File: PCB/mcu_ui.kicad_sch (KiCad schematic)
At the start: 32 parts, among them J5 UPDI, SW1 EC11E18244A5, SW2 BAND, SW3 STEP, SW4 MENU, U4 ATtiny3226-SU

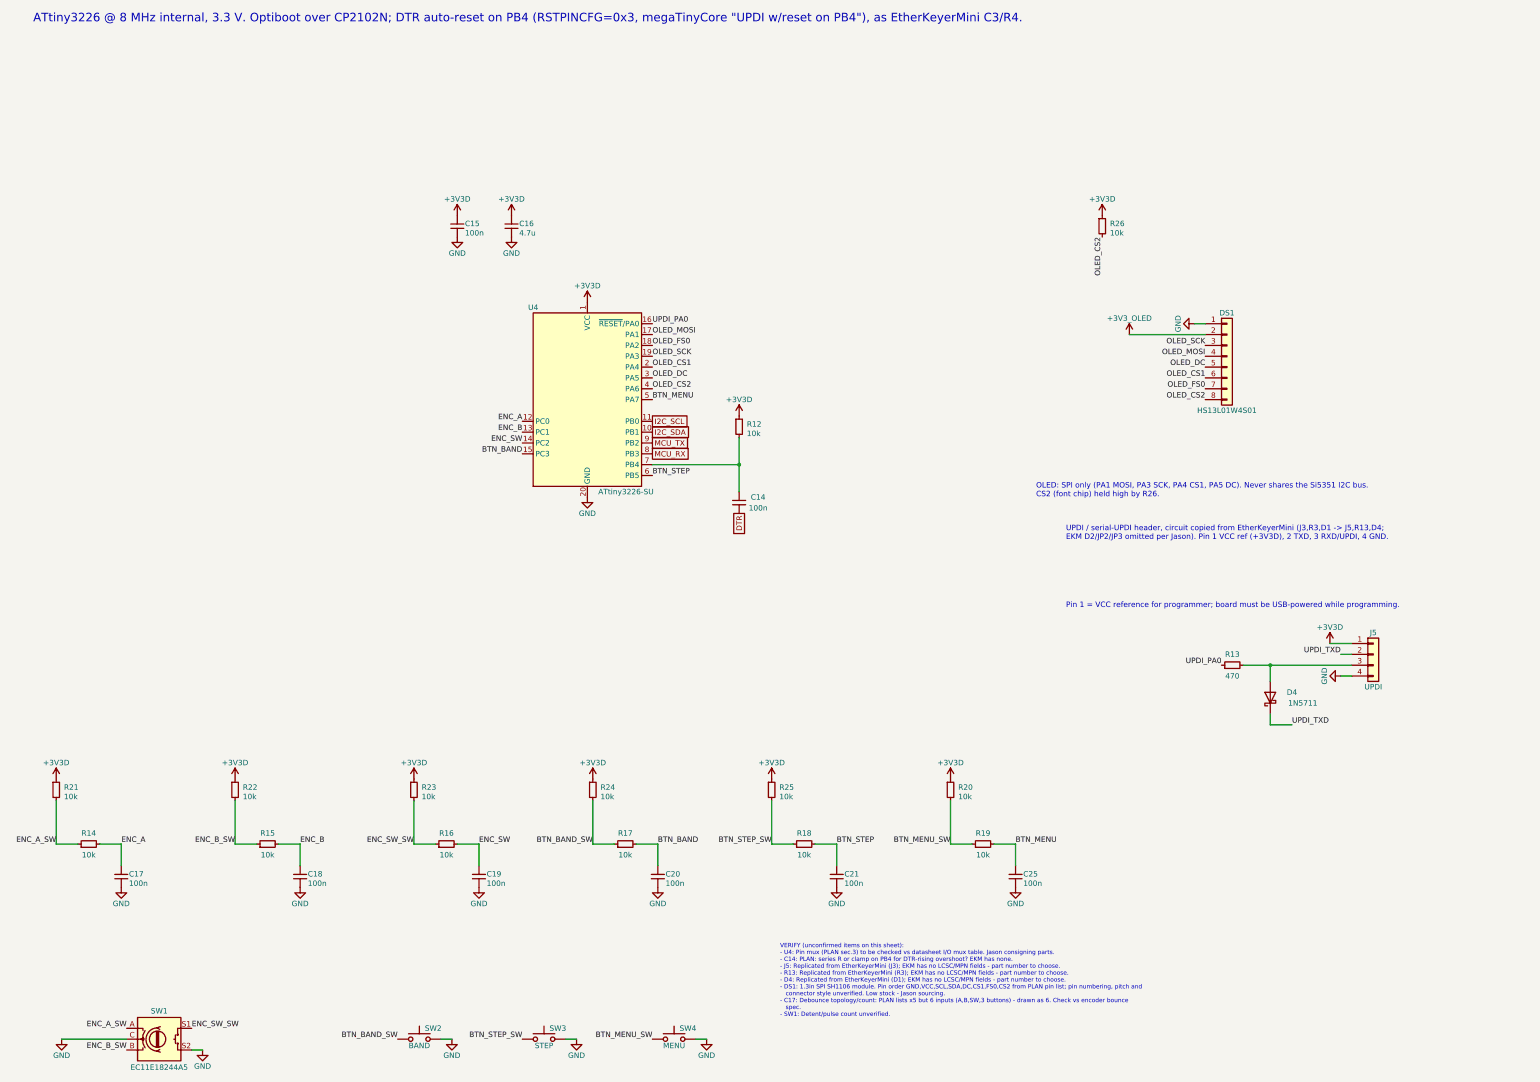
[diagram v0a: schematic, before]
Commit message: Schematic: US resistor symbols, decoupling caps at their ICs, drop finalized VERIFY notes
- Device:R_Small -> Device:R_Small_US on all 30 resistors (same pin geometry; refs/values/fields/footprints/LCSC unchanged)
- Move label-connected decoupling caps next to their ICs: C10/C11 + C12/C13 at U3, C15/C16 at U4, C4 at U2
- Add PCB placement notes by U1, U5, U3, U4, U2/X1 and DS1 (pins from netlist)
- Remove VERIFY note lines and VERIFY fields for items Jason finalized:
  J1 D1 C10 U3 FB2 DS1 C17 SW1 X1 C100 R101 L1 C105
- Netlist identical to 4963a6d; ERC 0 errors
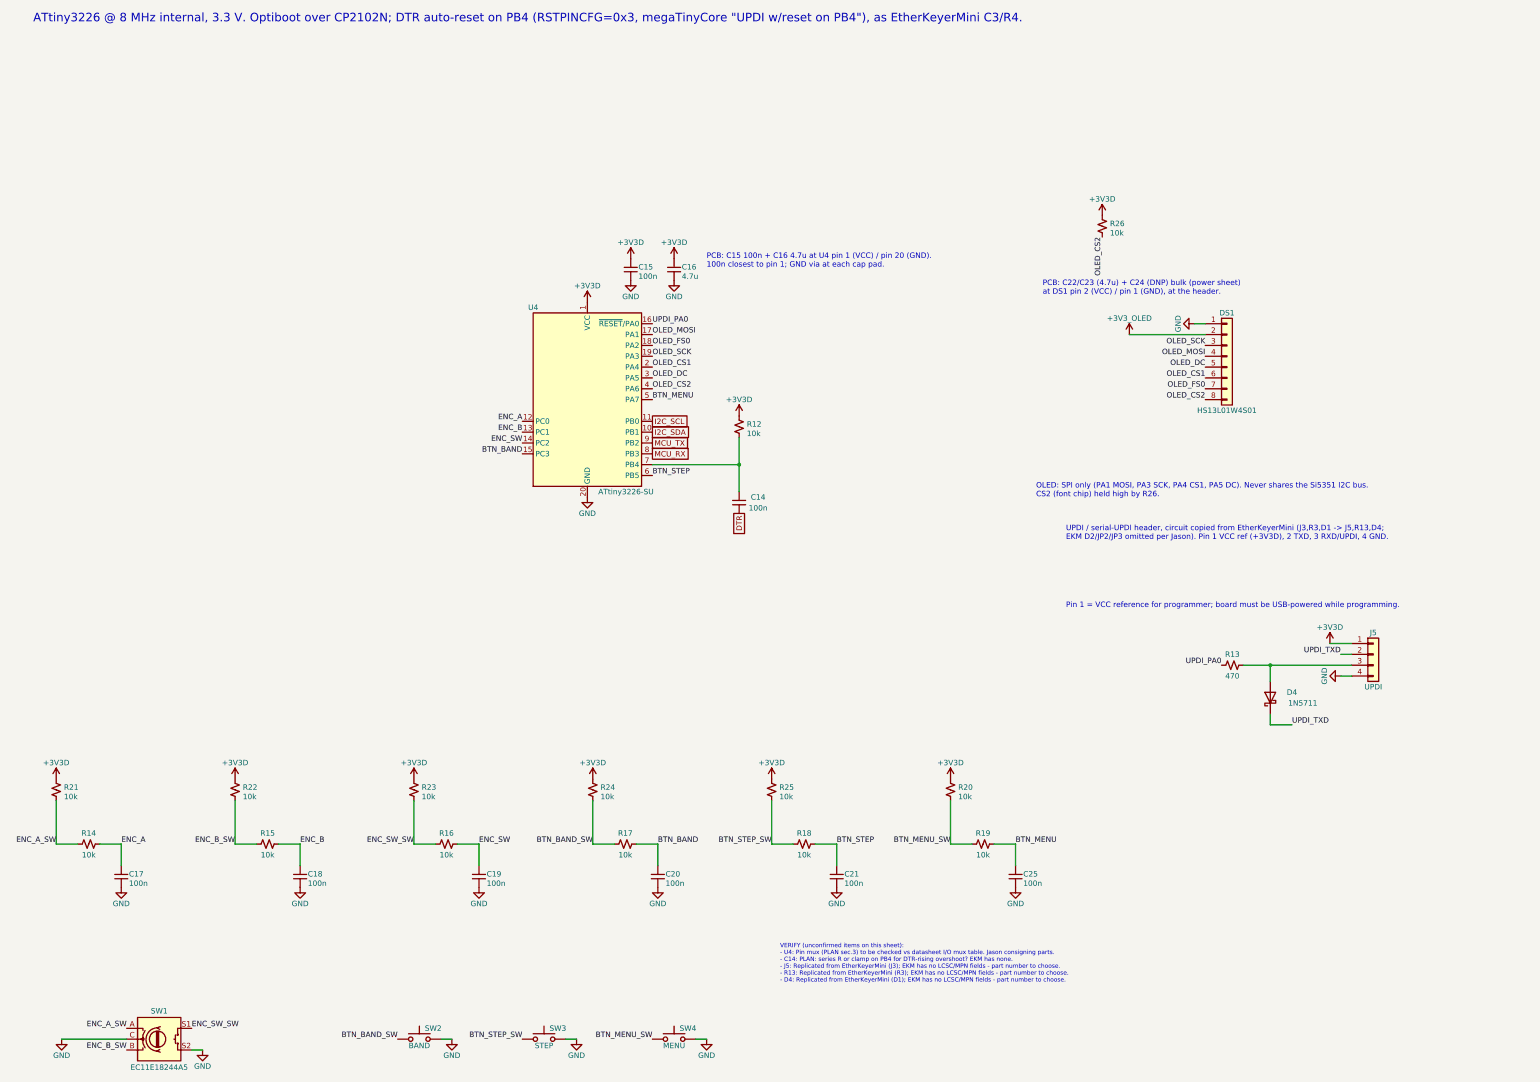
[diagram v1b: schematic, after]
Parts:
- C17: VERIFY Debounce topology/count: PLAN lists x5 but 6 inputs (A,B,SW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 -> (none)
- DS1: VERIFY 1.3in SPI SH1106 module. Pin order GND,VCC,SCL,SDA,DC,CS1,F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 -> (none)
- R12, R13, R14, R15, R16, R17, R18, R19, R20, R21, R22, R23, R24, R25, R26: symbol Device:R_Small -> Device:R_Small_US
- SW1: VERIFY Detent/pulse count unverified. -> (none)
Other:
- note added: "PCB: C15 100n + C16 4.7u at U4 pin 1 (VCC) / pin 20 (GND). 100n closest to pin 1; GND via at each cap pad."
- note added: "PCB: C22/C23 (4.7u) + C24 (DNP) bulk (power sheet) at DS1 pin 2 (VCC) / pin 1 (GND), at the header."
- moved on the sheet: C15, C16
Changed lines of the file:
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@@
 		)
 	)
-	(text "VERIFY (unconfirmed items on this sheet):\n- U4: Pin mux (PLAN sec.3) to be checked vs datasheet I/O mux table. Jason consigning parts.\n- C14: PLAN: series R or clamp on PB4 for DTR-rising overshoot? EKM has none.\n- J5: Replicated from EtherKeyerMini (J3); EKM has no LCSC/MPN fields - part number to choose.\n- R13: Replicated from EtherKeyerMini (R3); EKM has no LCSC/MPN fields - part number to choose.\n- D4: Replicated from EtherKeyerMini (D1); EKM has no LCSC/MPN fields - part number to choose.\n- DS1: 1.3in SPI SH1106 module. Pin order GND,VCC,SCL,SDA,DC,CS1,FS0,CS2 from PLAN pin list; pin numbering, pitch and\n   connector style unverified. Low stock - Jason sourcing.\n- C17: Debounce topology/count: PLAN lists x5 but 6 inputs (A,B,SW,3 buttons) - drawn as 6. Check vs encoder bounce\n   spec.\n- SW1: Detent/pulse count unverified."
+	(text "VERIFY (unconfirmed items on this sheet):\n- U4: Pin mux (PLAN sec.3) to be checked vs datasheet I/O mux table. Jason consigning parts.\n- C14: PLAN: series R or clamp on PB4 for DTR-rising overshoot? EKM has none.\n- J5: Replicated from EtherKeyerMini (J3); EKM has no LCSC/MPN fields - part number to choose.\n- R13: Replicated from EtherKeyerMini (R3); EKM has no LCSC/MPN fields - part number to choose.\n- D4: Replicated from EtherKeyerMini (D1); EKM has no LCSC/MPN fields - part number to choose."
 		(exclude_from_sim no)
 		(at 195 238 0)
@@
 		)
 	)
+	(text "PCB: C15 100n + C16 4.7u at U4 pin 1 (VCC) / pin 20 (GND).\n100n closest to pin 1; GND via at each cap pad."
+		(exclude_from_sim no)
+		(at 177.8 76.2 0)
+		(effects
+			(font
+				(size 1.27 1.27)
+			)
+			(justify left top)
+		)
+	)
+	(text "PCB: C22/C23 (4.7u) + C24 (DNP) bulk (power sheet)\nat DS1 pin 2 (VCC) / pin 1 (GND), at the header."
+		(exclude_from_sim no)
+		(at 256.54 82.55 0)
+		(effects
+			(font
+				(size 1.27 1.27)
+			)
+			(justify left top)
+		)
+	)
 	(junction
 		(at 185.42 125.73)
@@
 	(symbol
 		(lib_id "Device:C_Small")
-		(at 132.08 69.85 0)
+		(at 170.18 80.01 0)
 		(unit 1)
 		(body_style 1)
@@
 		(dnp no)
 		(property "Reference" "C16"
-			(at 133.88 69.25 0)
+			(at 171.98 79.41 0)
 			(show_name no)
 			(do_not_autoplace no)
@@
 		)
 		(property "Value" "4.7u"
-			(at 133.88 71.45 0)
+			(at 171.98 81.61 0)
 			(show_name no)
 			(do_not_autoplace no)
@@
 		)
 		(property "Footprint" "Capacitor_SMD:C_0805_2012Metric"
-			(at 132.08 69.85 0)
+			(at 170.18 80.01 0)
 			(hide yes)
 			(show_name no)
@@
 		)
 		(property "Datasheet" ""
-			(at 132.08 69.85 0)
+			(at 170.18 80.01 0)
 			(hide yes)
 			(show_name no)
@@
 		)
 		(property "Description" "Unpolarized capacitor, small symbol"
-			(at 132.08 69.85 0)
+			(at 170.18 80.01 0)
 			(hide yes)
 			(show_name no)
@@
 		)
 		(property "LCSC" "C1779"
-			(at 132.08 69.85 0)
+			(at 170.18 80.01 0)
 			(hide yes)
 			(show_name no)
@@
 		)
 		(property "MPN" "CL21A475KAQNNNE"
-			(at 132.08 69.85 0)
+			(at 170.18 80.01 0)
 			(hide yes)
 			(show_name no)
@@
 		)
 		(property "Manufacturer" "Samsung"
-			(at 132.08 69.85 0)
+			(at 170.18 80.01 0)
 			(hide yes)
 			(show_name no)
@@
 	)
 	(symbol
-		(lib_id "Device:R_Small")
+		(lib_id "Device:R_Small_US")
 		(at 300.99 172.72 90)
 		(unit 1)
@@
 	(symbol
 		(lib_id "power:+3V3")
-		(at 119.38 67.31 0)
+		(at 160.02 77.47 0)
 		(unit 1)
 		(body_style 1)
@@
 		(dnp no)
 		(property "Reference" "#PWR053"
-			(at 119.38 67.31 0)
+			(at 160.02 77.47 0)
 			(hide yes)
 			(show_name no)
@@
 		)
 		(property "Value" "+3V3D"
-			(at 119.38 63.5 0)
+			(at 160.02 73.66 0)
 			(show_name no)
 			(do_not_autoplace no)
@@
 		)
 		(property "Footprint" ""
-			(at 119.38 67.31 0)
+			(at 160.02 77.47 0)
 			(hide yes)
 			(show_name no)
@@
 		)
 		(property "Datasheet" ""
-			(at 119.38 67.31 0)
+			(at 160.02 77.47 0)
 			(hide yes)
 			(show_name no)
@@
 		)
 		(property "Description" ""
-			(at 119.38 67.31 0)
+			(at 160.02 77.47 0)
 			(show_name no)
 			(do_not_autoplace no)
@@
 	)
 	(symbol
-		(lib_id "Device:R_Small")
+		(lib_id "Device:R_Small_US")
 		(at 193.04 201.93 0)
 		(unit 1)
@@
 			)
 		)
-		(property "VERIFY" "1.3in SPI SH1106 module. Pin order GND,VCC,SCL,SDA,DC,CS1,FS0,CS2 from PLAN pin list; pin numbering, pitch and connector style unverified. Low stock - Jason sourcing."
-			(at 299.72 100.33 0)
-			(hide yes)
-			(show_name no)
-			(do_not_autoplace no)
-			(effects
-				(font
-					(size 1.27 1.27)
-				)
-			)
-		)
 		(pin "1"
 		)
@@
 	)
 	(symbol
-		(lib_id "Device:R_Small")
+		(lib_id "Device:R_Small_US")
 		(at 234.95 201.93 0)
 		(unit 1)
@@
 	)
 	(symbol
-		(lib_id "Device:R_Small")
+		(lib_id "Device:R_Small_US")
 		(at 33.02 214.63 90)
 		(unit 1)
@@
 	)
 	(symbol
-		(lib_id "Device:R_Small")
+		(lib_id "Device:R_Small_US")
 		(at 242.57 214.63 90)
 		(unit 1)
@@
 	(symbol
 		(lib_id "Device:C_Small")
-		(at 119.38 69.85 0)
+		(at 160.02 80.01 0)
 		(unit 1)
 		(body_style 1)
@@
 		(dnp no)
 		(property "Reference" "C15"
-			(at 121.18 69.25 0)
+			(at 161.82 79.41 0)
 			(show_name no)
 			(do_not_autoplace no)
@@
 		)
 		(property "Value" "100n"
-			(at 121.18 71.45 0)
+			(at 161.82 81.61 0)
 			(show_name no)
 			(do_not_autoplace no)
@@
 		)
 		(property "Footprint" "Capacitor_SMD:C_0805_2012Metric"
-			(at 119.38 69.85 0)
+			(at 160.02 80.01 0)
 			(hide yes)
 			(show_name no)
@@
 		)
 		(property "Datasheet" ""
-			(at 119.38 69.85 0)
+			(at 160.02 80.01 0)
 			(hide yes)
 			(show_name no)
@@
 		)
 		(property "Description" "Unpolarized capacitor, small symbol"
-			(at 119.38 69.85 0)
+			(at 160.02 80.01 0)
 			(hide yes)
 			(show_name no)
@@
 		)
 		(property "LCSC" "C49678"
-			(at 119.38 69.85 0)
+			(at 160.02 80.01 0)
 			(hide yes)
 			(show_name no)
@@
 		)
 		(property "MPN" "CC0805KRX7R9BB104"
-			(at 119.38 69.85 0)
+			(at 160.02 80.01 0)
 			(hide yes)
 			(show_name no)
@@
 		)
 		(property "Manufacturer" "YAGEO"
-			(at 119.38 69.85 0)
+			(at 160.02 80.01 0)
 			(hide yes)
 			(show_name no)
@@
 	)
 	(symbol
-		(lib_id "Device:R_Small")
+		(lib_id "Device:R_Small_US")
 		(at 25.4 201.93 0)
 		(unit 1)
@@
 	)
 	(symbol
-		(lib_id "Device:R_Small")
+		(lib_id "Device:R_Small_US")
 		(at 185.42 116.84 0)
 		(unit 1)
@@
 	)
 	(symbol
-		(lib_id "Device:R_Small")
+		(lib_id "Device:R_Small_US")
 		(at 151.13 201.93 0)
 		(unit 1)
@@
 	)
 	(symbol
-		(lib_id "Device:R_Small")
+		(lib_id "Device:R_Small_US")
 		(at 116.84 214.63 90)
 		(unit 1)
@@
 	)
 	(symbol
-		(lib_id "Device:R_Small")
+		(lib_id "Device:R_Small_US")
 		(at 270.51 69.85 0)
 		(unit 1)
@@
 	(symbol
 		(lib_id "power:GND")
-		(at 119.38 72.39 0)
+		(at 160.02 82.55 0)
 		(unit 1)
 		(body_style 1)
@@
 		(dnp no)
 		(property "Reference" "#PWR054"
-			(at 119.38 72.39 0)
+			(at 160.02 82.55 0)
 			(hide yes)
 			(show_name no)
@@
 		)
 		(property "Value" "GND"
-			(at 119.38 76.2 0)
+			(at 160.02 86.36 0)
 			(show_name no)
 			(do_not_autoplace no)
@@
 		)
 		(property "Footprint" ""
-			(at 119.38 72.39 0)
+			(at 160.02 82.55 0)
 			(hide yes)
 			(show_name no)
@@
 		)
 		(property "Datasheet" ""
-			(at 119.38 72.39 0)
+			(at 160.02 82.55 0)
 			(hide yes)
 			(show_name no)
@@
 		)
 		(property "Description" ""
-			(at 119.38 72.39 0)
+			(at 160.02 82.55 0)
 			(show_name no)
 			(do_not_autoplace no)
@@
 	)
 	(symbol
-		(lib_id "Device:R_Small")
+		(lib_id "Device:R_Small_US")
 		(at 67.31 201.93 0)
 		(unit 1)
@@
 	(symbol
 		(lib_id "power:GND")
-		(at 132.08 72.39 0)
+		(at 170.18 82.55 0)
 		(unit 1)
 		(body_style 1)
@@
 		(dnp no)
 		(property "Reference" "#PWR056"
-			(at 132.08 72.39 0)
+			(at 170.18 82.55 0)
 			(hide yes)
 			(show_name no)
@@
 		)
 		(property "Value" "GND"
-			(at 132.08 76.2 0)
+			(at 170.18 86.36 0)
 			(show_name no)
 			(do_not_autoplace no)
@@
 		)
 		(property "Footprint" ""
-			(at 132.08 72.39 0)
+			(at 170.18 82.55 0)
 			(hide yes)
 			(show_name no)
@@
 		)
 		(property "Datasheet" ""
-			(at 132.08 72.39 0)
+			(at 170.18 82.55 0)
 			(hide yes)
 			(show_name no)
@@
 		)
 		(property "Description" ""
-			(at 132.08 72.39 0)
+			(at 170.18 82.55 0)
 			(show_name no)
 			(do_not_autoplace no)
@@
 			)
 		)
-		(property "VERIFY" "Debounce topology/count: PLAN lists x5 but 6 inputs (A,B,SW,3 buttons) - drawn as 6. Check vs encoder bounce spec."
-			(at 40.64 222.25 0)
-			(hide yes)
-			(show_name no)
-			(do_not_autoplace no)
-			(effects
-				(font
-					(size 1.27 1.27)
-				)
-			)
-		)
 		(pin "1"
 		)
@@
 	(symbol
 		(lib_id "power:+3V3")
-		(at 132.08 67.31 0)
+		(at 170.18 77.47 0)
 		(unit 1)
 		(body_style 1)
@@
 		(dnp no)
 		(property "Reference" "#PWR055"
-			(at 132.08 67.31 0)
+			(at 170.18 77.47 0)
 			(hide yes)
 			(show_name no)
@@
 		)
 		(property "Value" "+3V3D"
-			(at 132.08 63.5 0)
+			(at 170.18 73.66 0)
 			(show_name no)
 			(do_not_autoplace no)
@@
 		)
 		(property "Footprint" ""
-			(at 132.08 67.31 0)
+			(at 170.18 77.47 0)
 			(hide yes)
 			(show_name no)
@@
 		)
 		(property "Datasheet" ""
-			(at 132.08 67.31 0)
+			(at 170.18 77.47 0)
 			(hide yes)
 			(show_name no)
@@
 		)
 		(property "Description" ""
-			(at 132.08 67.31 0)
+			(at 170.18 77.47 0)
 			(show_name no)
 			(do_not_autoplace no)
@@
 			)
 		)
-		(property "VERIFY" "Detent/pulse count unverified."
-			(at 49.53 260.35 0)
-			(hide yes)
-			(show_name no)
-			(do_not_autoplace no)
-			(effects
-				(font
-					(size 1.27 1.27)
-				)
-			)
-		)
 		(pin "A"
 		)
@@
 	)
 	(symbol
-		(lib_id "Device:R_Small")
+		(lib_id "Device:R_Small_US")
 		(at 109.22 201.93 0)
 		(unit 1)
@@
 	)
 	(symbol
-		(lib_id "Device:R_Small")
+		(lib_id "Device:R_Small_US")
 		(at 158.75 214.63 90)
 		(unit 1)
@@
 	)
 	(symbol
-		(lib_id "Device:R_Small")
+		(lib_id "Device:R_Small_US")
 		(at 74.93 214.63 90)
 		(unit 1)
@@
 	)
 	(symbol
-		(lib_id "Device:R_Small")
+		(lib_id "Device:R_Small_US")
 		(at 200.66 214.63 90)
 		(unit 1)

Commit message: Resolve VERIFY directives: R9 to VIO, R29 on PB4, OLED bulk, SMD UPDI parts, 4.7k I2C, 0805 0R, Etherkit SMA footprint
- R9 /RST pull-up moved from +5V to CP_VDD (CP2102N DS 2.1, Table 3.10)
- New R29 1k (C21190) between C14 and PB4 to limit DTR-rise injection current (ATtiny3226 DS Table 33-1)
- C24 fitted 22u 1206 (C12891); C22/C23 kept 2x4.7u
- R13 0603 C23179, D4 1N5711W SOD-123 C154843, J5 1x4 pin header C124378
- R27/R28 4.7k C17673; R100/R120/R140 0805 0R C17477; R101/R121/R141 LCSC C17437 (DNP)
- J2-J4 footprint EtherkitKicadLibrary:SMA-ENDLAUNCH
- H1-H4 and solder jumpers excluded from BOM
- Finalized VERIFY notes removed from sheets; VERIFY.md items ticked with KiCad EE notes
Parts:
- added R29: 1k, Resistor_SMD:R_0603_1608Metric, symbol Device:R_Small_US
- D4: value 1N5711 -> 1N5711W; footprint Diode_THT:D_DO-35_SOD27_P7.62mm_Horizontal -> Diode_SMD:D_SOD-123; LCSC (none) -> C154843; MPN (none) -> 1N5711W-7-F; Manufacturer (none) -> Diodes Incorporated
- J5: footprint Connector_PinSocket_2.54mm:PinSocket_1x04_P2.54mm_Vertical -> Connector_PinHeader_2.54mm:PinHeader_1x04_P2.54mm_Vertical; LCSC (none) -> C124378; MPN (none) -> B-2100S04P-A110; Manufacturer (none) -> Ckmtw
- R13: footprint Resistor_THT:R_Axial_DIN0207_L6.3mm_D2.5mm_P2.54mm_Vertical -> Resistor_SMD:R_0603_1608Metric; LCSC (none) -> C23179; MPN (none) -> 0603WAF4700T5E; Manufacturer (none) -> UNI-ROYAL
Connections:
- net at R12.2, U4.7 (PB4): now also R29.1; no longer C14.2
- new net: C14.2, R29.2
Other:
- note removed: "VERIFY (unconfirmed items on this sheet): - U4: Pin mux (PLAN sec.3) to be checked vs datasheet I/O mux table. Jason consigning parts. - C14: PLAN: series R or clamp on PB4 for DTR-rising overshoot? EKM has none. - J5: Replicated from EtherKeyerMini (J3); EKM has no LCSC/MPN fields - part number to choose. - R13: Replicated from EtherKeyerMini (R3); EKM has no LCSC/MPN fields - part number to cho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"
- moved on the sheet: C14

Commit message: Pre-layout: project-local Etherkit libs (ERC 0/0), DS1/J2-J4/X1 fit review, title block, clear finalized VERIFY fields, LPF closed
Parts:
- C14: VERIFY PLAN: series R or clamp on PB4 for DTR-rising overshoot? EK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 -> (none)
- D4: VERIFY Replicated from EtherKeyerMini (D1); EKM has no LCSC/MPN fi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 -> (none)
- J5: VERIFY Replicated from EtherKeyerMini (J3); EKM has no LCSC/MPN fi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 -> (none)
- R13: VERIFY Replicated from EtherKeyerMini (R3); EKM has no LCSC/MPN fi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 -> (none)
- U4: VERIFY Pin mux (PLAN sec.3) to be checked vs datasheet I/O mux tab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 -> (none)
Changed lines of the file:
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@@
 		(rev "A")
 		(company "Etherkit / NT7S")
-		(comment 1 "Draft schematic, not reviewed. See VERIFY notes.")
+		(comment 1 "Draft schematic, not reviewed. Open items: docs/VERIFY.md")
 	)
 	(text "UPDI / serial-UPDI header, circuit copied from EtherKeyerMini (J3,R3,D1 -> J5,R13,D4;\nEKM D2/JP2/JP3 omitted per Jason). Pin 1 VCC ref (+3V3D), 2 TXD, 3 RXD/UPDI, 4 GND."
@@
 			)
 		)
-		(property "VERIFY" "Replicated from EtherKeyerMini (R3); EKM has no LCSC/MPN fields - part number to choose."
-			(at 300.99 172.72 0)
-			(hide yes)
-			(show_name no)
-			(do_not_autoplace no)
-			(effects
-				(font
-					(size 1.27 1.27)
-				)
-			)
-		)
 		(property "LCSC" "C23179"
 			(at 300.99 172.72 0)
@@
 			)
 		)
-		(property "VERIFY" "Replicated from EtherKeyerMini (D1); EKM has no LCSC/MPN fields - part number to choose."
-			(at 309.88 180.34 0)
-			(hide yes)
-			(show_name no)
-			(do_not_autoplace no)
-			(effects
-				(font
-					(size 1.27 1.27)
-				)
-			)
-		)
 		(property "LCSC" "C154843"
 			(at 309.88 180.34 0)
@@
 			)
 		)
-		(property "VERIFY" "Replicated from EtherKeyerMini (J3); EKM has no LCSC/MPN fields - part number to choose."
-			(at 334.01 170.18 0)
-			(hide yes)
-			(show_name no)
-			(do_not_autoplace no)
-			(effects
-				(font
-					(size 1.27 1.27)
-				)
-			)
-		)
 		(property "LCSC" "C124378"
 			(at 334.01 170.18 0)
@@
 			)
 		)
-		(property "VERIFY" "PLAN: series R or clamp on PB4 for DTR-rising overshoot? EKM has none."
-			(at 185.42 139.7 0)
-			(hide yes)
-			(show_name no)
-			(do_not_autoplace no)
-			(effects
-				(font
-					(size 1.27 1.27)
-				)
-			)
-		)
 		(pin "1"
 		)
@@
 			(at 149.86 110.49 0)
 			(hide yes)
-			(show_name no)
-			(do_not_autoplace no)
-			(effects
-				(font
-					(size 1.27 1.27)
-				)
-			)
-		)
-		(property "VERIFY" "Pin mux (PLAN sec.3) to be checked vs datasheet I/O mux table. Jason consigning parts."
-			(at 149.86 110.49 0)
-			(hide yes)
